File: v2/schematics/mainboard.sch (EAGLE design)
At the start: 145 parts, among them IC1 TEENSY 3.6, IC10 UDN2981A, IC2 LM393, IC3 DRV8835, IC4 LM2596S-ADJ, IC5 LM2596S-5.0, IC6 PCF8574P, IC7 PCF8574P, IC8 LD1117A, IC9 TSOP34830, J1 Servo_1, J10 Uart_5, J11 Servo_3, J12 USB_Host, J13 BNO055, J14 I2C_0 / Uart_3, J15 SPI_1, J16 SPI_2, J17 Uart_6, J18 Maus_select, J19 Erw_analog, J2 Servo_2, J20 Erw_PWM, J21 Erw_GPIO, J23 Uart_1, J24 I2C_3, J3 Erw_Pow, J30 H-Bridge Mode, J4 Uart_2, J5 BPS, J6 Erw_ENA, J7 I2C_2, J8 I2C_Display, J9 RPI_SPI0, Q2 IRL3103, SW1 TL36WO, U1 CNY70, U2 BLE-HM-10, U3 BSS138, U4 BSS138, U5 BSS138, X1 Bat

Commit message: bugfixes for wrong voltage dividers
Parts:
- removed C12: 1uF, rcl:C-EU025-025X050
- removed R47, R48: 2k2, rcl:R-EU_0204/2V
- removed U2: BLE-HM-10, BLE_HM-10:RANDOM-PARTS_BLE-HM-10
- R49, R50: value 3k9 -> 100k
- R51: value 2k2 -> 100k
- R52: value 3k9 -> 180k
- ST7, ST8, ST9: device pinhead_ts:PINHD-1X10 -> pinhead_ts:PS25-10PS25-10
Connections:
- removed net BLE_RESET: J10.4, U2.RESETB
- removed net MLINKS_3V3: IC1.18/A4/PWM/T/SDA0, R47.1, R50.1
- removed net MRECHTS_3V3: IC1.19/A5/PWM/T/SCL0, R48.1, R49.1
- net +3V3: no longer C12.1, U2.3.3V
- net +5V: now also J10.2
- net GND: no longer C12.2, U2.GND1
- net MLINKS: now also IC1.18/A4/PWM/T/SDA0, R50.1; no longer R47.2
- net MRECHTS: now also IC1.19/A5/PWM/T/SCL0, R49.1; no longer R48.2
- net RX5: now also J10.3; no longer J10.2, U2.UART_TX
- net TX5: now also J10.4; no longer J10.3, U2.UART_RX
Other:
- note added: "0.4"
- note added: "BLE / WiFi Modul? Oder Anschluss dafuer?"
- note removed: "0.3"
- note removed: "Interruptfaehigkeit der Eingaenge pruefen!"
- moved on the sheet: J10, J17, J23, J4, J5, R49, R50

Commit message: cleanup of schematic, bugfix wheel encoder circuit
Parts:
- removed L3: 47u, inductors:09HCP
- removed Q2: IRL3103, transistor-power:IRF740
- removed ST7: Maussensor, pinhead_ts:PS25-10PS25-10
- removed ST8: Sensoren L, pinhead_ts:PS25-10PS25-10
- removed ST9: Sensoren R, pinhead_ts:PS25-10PS25-10
- removed SV1: RPI_Interface, con-harting-ml:ML26
- added C12: 100nF, rcl:C-EU025-025X050
- added C18: 220uF, rcl:CPOL-EUE2-5
- added C21, C22: 220n, rcl:C-EU025-025X050
- added C23, C24, C25, C27: 1u, rcl:C-EU025-025X050
- added C26: 220u, rcl:CPOL-EUE2.5-6
- added C28, C30: 2.2nF, rcl:C-EU025-025X050
- added C29, C31: 6.8nF, rcl:C-EU025-025X050
- added C3: 1nF, rcl:C-EU025-025X050
- added IC11: ESP01, esp8266modules:ESP01
- added IC12: MAX803TEXR, maxim-10:MAX803TEXR
- added J22: Erw_GPIO, pinhead_ts:PINHD-1X4
- added J25: Bat_In, pinhead_ts:PINHD-1X2
- added J26: SWD, pinhead_ts:PINHD-1X6
- added J27: SPEAKER, pinhead_ts:PINHD-1X2
- added J28: AUDIO, pinhead_ts:PINHD-1X2
- added J29: GAIN_0, pinhead_ts:PINHD-1X3
- added J31: SWD_KL02, pinhead_ts:PINHD-1X2
- added J32: SWD_KL02, pinhead_ts:PINHD-1X2/90
- added L1: 47u, inductors:09HCP
- added R47, R48: 330, rcl:R-EU_0204/2V
- added ST1: Motor L, pinhead_ts:PINHD-1X2/90
- added ST4: Sensoren R, pinhead_ts:PS25-10PS25-10
- added ST5: RPI_Interface, con-harting-ml:ML26
- added ST6: Maussensor, pinhead_ts:PS25-10PS25-10
- added U2: CNY70, cny70:CNY70
- added U6: TPA3106D1, user:TPA3106D1
- C1: value 220uF -> 680uF; device rcl:CPOL-EUE2-5 -> rcl:CPOL-EUE5-10.5
- C10: value 220u -> 100nF; device rcl:CPOL-EUE5-10.5 -> rcl:C-EU025-025X050
- C11: value 1nF -> 100nF
- C13: value 22uF -> 220uF; device rcl:C-EU025-025X050 -> rcl:CPOL-EUE2-5
- C15: value 220uF -> 100nF; device rcl:CPOL-EUE2-5 -> rcl:C-EU025-025X050
- C16: value 100nF -> 100uF; device rcl:C-EU025-025X050 -> rcl:CPOL-EUE2-5
- C19: value 100uF -> 1u; device rcl:CPOL-EUE2-5 -> rcl:C-EU025-025X050
- C2: value 100nF -> 22uF
- C20: value 10uF -> 10n; device rcl:CPOL-EUE2.5-5 -> rcl:C-EU025-025X050
- C4: value 100nF -> 220u; device rcl:C-EU025-025X050 -> rcl:CPOL-EUE5-10.5
- C6: value 680uF -> 22uF; device rcl:CPOL-EUE5-10.5 -> rcl:C-EU025-025X050
- C8: value 22uF -> 100nF
- C9: value 100nF -> 10uF; device rcl:C-EU025-025X050 -> rcl:CPOL-EUE2.5-5
- IC1: value TEENSY 3.6 -> LM2596S-ADJ; device Teensy_3_6:TEENSY3_6--ALLPINS -> linear:LM2596S
- IC10: value UDN2981A -> TSOP34830; device uln-udn:UDN2981A -> vishay-1:TSOP34830
- IC2: value LM393 -> LM2596S-5.0; device linear:LM393N -> linear:LM2596S; SPICEPREFIX J -> (none)
- IC3: value DRV8835 -> LD1117A; device pololu:POLOLU_MOTOR_DRV8835THROUGHHOLE -> LD1117:LD1117
- IC4: value LM2596S-ADJ -> DRV8835; device linear:LM2596S -> pololu:POLOLU_MOTOR_DRV8835THROUGHHOLE
- IC5: value LM2596S-5.0 -> LM393; device linear:LM2596S -> linear:LM393N; SPICEPREFIX (none) -> J
- IC6: value PCF8574P -> TEENSY 3.6; device micro-philips:PCF8574P -> Teensy_3_6:TEENSY3_6--ALLPINS
- IC8: value LD1117A -> PCF8574P; device LD1117:LD1117 -> micro-philips:PCF8574P
- IC9: value TSOP34830 -> UDN2981A; device vishay-1:TSOP34830 -> uln-udn:UDN2981A
- J1: value Servo_1 -> Erw_Pow; device pinhead_ts:PINHD-1X3 -> pinhead_ts:PINHD-1X4
- J10: value Uart_5 -> I2C_0
- J11: value Servo_3 -> I2C_3
- J12: value USB_Host -> Uart_1
- J13: value BNO055 -> Uart_6; device pinhead_ts:PINHD-1X6 -> pinhead_ts:PINHD-1X4
- J14: value I2C_0 / Uart_3 -> USB_Host
- J15: value SPI_1 -> BPS; device pinhead_ts:PINHD-1X6 -> pinhead_ts:PINHD-1X3
- J16: value SPI_2 -> RPI_SPI0; device pinhead_ts:PINHD-1X5 -> pinhead_ts:PINHD-1X6
- J17: value Uart_6 -> SPI_1; device pinhead_ts:PINHD-1X4 -> pinhead_ts:PINHD-1X6
- J18: value Maus_select -> SPI_2; device pinhead_ts:PINHD-1X3 -> pinhead_ts:PINHD-1X5
- J2: value Servo_2 -> H-Bridge Mode; device pinhead_ts:PINHD-1X4 -> pinhead_ts:PINHD-1X2
- J20: value Erw_PWM -> Erw_Servo; device pinhead_ts:PINHD-1X4 -> pinhead_ts:PINHD-1X3
- J21: value Erw_GPIO -> Erw_PWM; SPICEPREFIX E -> (none)
- J23: value Uart_1 -> Erw_ENA; device pinhead_ts:PINHD-1X4 -> pinhead_ts:PINHD-1X6
- J24: value I2C_3 -> ESP01 Prog; device pinhead_ts:PINHD-1X4 -> pinhead_ts:PINHD-1X3
- J3: value Erw_Pow -> Servo_1; device pinhead_ts:PINHD-1X5 -> pinhead_ts:PINHD-1X3
- J30: value H-Bridge Mode -> GAIN_1; device pinhead_ts:PINHD-1X2 -> pinhead_ts:PINHD-1X3
- J4: value Uart_2 -> Servo_2
- J5: value BPS -> Servo_3; device pinhead_ts:PINHD-1X3 -> pinhead_ts:PINHD-1X4
- J6: value Erw_ENA -> Maus_select; device pinhead_ts:PINHD-1X6 -> pinhead_ts:PINHD-1X3
- J7: value I2C_2 -> BNO055
- J8: value I2C_Display -> Uart_2
- J9: value RPI_SPI0 -> I2C_Display; device pinhead_ts:PINHD-1X6 -> pinhead_ts:PINHD-1X4
- LED1: value blau -> 6V
- LED10: value 6V -> tuerkis
- LED11: value 3.3V -> weiss
- LED2: value blau -> 5V
- LED3: value rot -> 3.3V
- LED4: value orange -> blau
- LED5: value gelb -> blau
- LED6: value gruen -> rot
- LED7: value tuerkis -> orange
- LED8: value weiss -> gelb
- LED9: value 5V -> gruen
- R1, R37, R38, R8: value 4k7 -> 100k
- R10: value 330 -> 100
- R11: value 330 -> 47k
- R12, R13: value 330 -> 470k
- R14: value 330 -> 5k; device rcl:R-EU_0204/2V -> rcl:R-TRIMM64W
- R15: value 330 -> 10k
- R16: value 330 -> 1M
- R17: value 3K9 0.1% -> 10k; device rcl:R-EU_0204/2V -> rcl:R-EU_0204/7
- R18: value 22k -> 15k
- R19: value 5k -> 10k; device rcl:R-TRIMM64W -> rcl:R-EU_0204/2V
- R2: value 100k -> 3K9 0.1%
- R21: value 470k -> 10k
- R22: value 470k -> 1M
- R23: value 210 -> 10k
- R24: value 210 -> 15k
- R25: value 180 -> 10k
- R26: value 180 -> 6,8 2W; device rcl:R-EU_0204/2V -> rcl:R-EU_0204/7
- R27: value 100 -> 4k7
- R28: value 6,8 2W -> 4k7; device rcl:R-EU_0204/7 -> rcl:R-EU_0204/2V
- R29: value 1K 0.1% -> 4k7
- R3: value 100 -> 1K 0.1%
- R30: value 390 -> 210; device resistor:R-EU_0204/2V -> rcl:R-EU_0204/2V
- R31: value 4k7 -> 210
- R32: value 1k8 -> 180
- R33: value 100k -> 180
- R34, R35: value 10k -> 47k
- R36: value 10k -> 100; device rcl:R-EU_0204/7 -> rcl:R-EU_0204/2V
- R39: value 10k -> 1k8
- R4: value 330 -> 390
- R40: value 1k8 -> 4k7; device rcl:R-EU_0204/7 -> rcl:R-EU_0204/2V
- R41: value 1M -> 1k8
- R42: value 1M -> 4k7
- R43: value 10k -> 100k
- R44: value 10k -> 180k
- R45: value 4k7 -> 330; device rcl:R-EU_0204/7 -> rcl:R-EU_0204/2V
- R46: value 4k7 -> 330
- R49, R50, R51: value 100k -> 330
- R5: value 47k -> 330; device rcl:R-EU_0204/2V -> resistor:R-EU_0204/2V
- R52: value 180k -> 330
- R53: value 10k -> 4k7
- R54: value 10k -> 4k7; device rcl:R-EU_0204/7 -> rcl:R-EU_0204/2V
- R55, R56: value 15k -> 10k
- R57: value 120 -> 10k; device resistor:R-EU_0204/2V -> rcl:R-EU_0204/2V
- R59: value 10k -> 5K; device rcl:R-EU_0204/2V -> rcl:R-TRIMM64W
- R6: value 47k -> 120; device rcl:R-EU_0204/2V -> resistor:R-EU_0204/2V
- R60: value 1k -> 100K
- R7: value 47k -> 1k
- R9: value 330 -> 22k
- ST2: value Motor L -> Motor R
- ST3: value Motor R -> Sensoren L; device pinhead_ts:PINHD-1X2/90 -> pinhead_ts:PS25-10PS25-10
- SW1: value TL36WO -> TL32PO; device switch:TL36WO -> switch:TL32PO
- U1: value CNY70 -> IRL3103; device cny70:CNY70 -> transistor-power:IRF740; SPICEPREFIX E -> (none)
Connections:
- removed net A21_DAC0: IC1.DAC0, J19.2
- removed net PWM_ERW: IC1.2/PWM, J20.1
- removed net SCL2: IC1.3/PWM/SCL2/CAN0TX, IC6.SCL, IC7.SCL, J7.6, R8.1, SV1.21, U4.S
- removed net SCL2_5V: J13.5, J8.4, R58.1, SV1.9, U4.D
- removed net SDA2: IC1.4/PWM/SDA2/CAN0RX, IC6.SDA, IC7.SDA, J7.5, R31.1, SV1.19, U3.S
- removed net SDA2_5V: J13.4, J8.3, R59.1, SV1.7, U3.D
- new net 3V3_TEENSY: IC12.VCC, IC6.3V3, J26.1
- new net AUDIO_OUT: IC6.DAC0, J19.2, J28.1
- new net BSN1: C21.1, U6.BSN
- new net BSP1: C22.1, U6.BSP
- new net ESP_GPIO0: IC11.GPIO0, J24.2
- new net ESP_GPIO2: IC11.GPIO2, J24.1
- new net GAIN0: J29.2, U6.GAIN0
- new net GAIN1: J30.2, U6.GAIN1
- new net INN: C24.1, U6.INN
- new net INP: C25.1, U6.INP
- new net KL02_DC: J31.1, J32.1
- new net KL02_DD: J31.2, J32.2
- new net LINE_IN: J28.2, R59.A
- new net N$163: C25.2, R59.S
- new net N$90: U6.FAULT, U6.MUTE
- new net OUTN: C21.2, J27.1, U6.OUTN0, U6.OUTN1
- new net OUTP: C22.2, J27.2, U6.OUTP0, U6.OUTP1
- new net PWM_ERW1: IC6.2/PWM, J21.2
- new net PWM_ERW2: IC6.3/PWM/SCL2/CAN0TX, J21.3
- new net PWM_ERW3: IC6.4/PWM/SDA2/CAN0RX, J21.4
- new net ROSC: R60.2, U6.ROSC
- new net SCL0_5V: J7.5, J9.4, R56.1, ST5.9, U4.D
- new net SDA0_5V: J7.4, J9.3, R55.1, ST5.7, U3.D
- new net SWCLK: IC6.DC, J26.5
- new net SWDIO: IC6.DD, J26.6
- new net SWD_EN: IC6.DE, J26.4
- new net VBYP: C19.1, U6.VBYP
- new net VCLAMP1: C23.1, U6.VCLAMP
- new net VREG: C20.1, J29.1, J30.1, U6.MSTR/SLV, U6.VREG
- net +3V3: now also C17.1, C9.+, IC10.VS, IC11.CH_PD, IC11.VCC, IC3.VOUT, J1.2, J15.3, J6.3, R11.1, R12.1, R13.1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; no longer C20.+, IC8.VOUT, IC9.VS, J18.3, J3.2, J5.3, R1.1, R19.E, R21.1, R22.1, R31.2, R35.2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
- net +5V: now also C12.1, C13.+, C15.1, C16.+, C18.+, C8.1, IC2.FB, IC3.VIN, IC4.VCC, IC5P.V+, IC6.VIN, IC8.A0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; no longer C1.+, C15.+, C19.+, C2.1, C4.1, C9.1, IC1.VIN, IC10.VS, IC2P.V+, IC3.VCC, IC5.FB, IC6.VDD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
- net +6V: now also C3.1, C4.+, IC4.VIN, J1.3, L1.2, R2.2, R26.1, R4.1; no longer C10.+, C11.1, IC3.VIN, J3.3, L2.2, R17.2, R28.1, R30.1
- net A22_DAC1: now also IC6.DAC1; no longer IC1.DAC1
- net ABSTL: now also R39.2, ST3.4; no longer R32.2, ST8.4
- net ABSTL_3V3: now also IC6.A11, R39.1, R40.1; no longer IC1.A11, R32.1, R46.1
- net ABSTR: now also R41.2, ST4.4; no longer R40.2, ST9.4
- net ABSTR_3V3: now also IC6.A10, R41.1, R42.1; no longer IC1.A10, R40.1, R45.1
- net BAT+: now also R1.1, X1-2.KL; no longer R33.1, X1-1.KL
- net BAT-: now also U1.D, X1-1.KL; no longer Q2.D, X1-2.KL
- net BAT_IN: now also C1.+, C2.1, C26.+, C27.1, C6.1, IC1.IN, IC2.IN, J25.1, R8.1, U6.!SHUTDOWN, U6.AVCC, U6.PVCC0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; no longer C13.1, C6.+, C8.1, IC4.IN, IC5.IN, J3.5, R2.1
- net BAT_IN_FB: now also IC6.39/A20/ALT-MISO0, R7.1; no longer IC1.39/A20/ALT-MISO0, R60.1
- net BPS: now also IC6.51/MISO2, J15.1; no longer IC1.51/MISO2, J5.1
- net CS0: now also IC6.15/A1/CS0-4/T, ST5.8; no longer IC1.15/A1/CS0-4/T, SV1.8
- net CS1: now also IC6.31/A12/PWM/RX4/CS1-0, J17.3; no longer IC1.31/A12/PWM/RX4/CS1-0, J15.3
- net CS2: now also IC6.43/CS2-0, J18.2; no longer IC1.43/CS2-0, J16.2
- net DRV_ABSTAND: now also IC9.O1, ST3.3, ST4.3; no longer IC10.O1, ST8.3, ST9.3
- net DRV_ERW_1: now also IC9.O7, J23.4; no longer IC10.O7, J6.4
- net DRV_ERW_2: now also IC9.O8, J23.6; no longer IC10.O8, J6.6
- net DRV_KANTLED: now also IC9.O4, R32.2, R33.1; no longer IC10.O4, R25.2, R26.1
- net DRV_KLAPPLED: now also IC9.O5, R10.2; no longer IC10.O5, R27.2
- net DRV_MAUS: now also IC9.O6, ST6.9; no longer IC10.O6, ST7.9
- net DRV_RADLED: now also IC9.O2, R30.2, R31.1; no longer IC10.O2, R23.2, R24.1
- net DRV_SCHRANKE: now also IC9.O3, ST3.7; no longer IC10.O3, ST8.7
- net ENA_ABSTAND: now also IC8.P0, IC9.I1; no longer IC10.I1, IC7.P0
- net ENA_ERW_1: now also IC8.P6, IC9.I7, J23.3; no longer IC10.I7, IC7.P6, J6.3
- net ENA_ERW_2: now also IC8.P7, IC9.I8, J23.5; no longer IC10.I8, IC7.P7, J6.5
- net ENA_KANTLED: now also IC8.P3, IC9.I4; no longer IC10.I4, IC7.P3
- net ENA_KLAPPLED: now also IC8.P4, IC9.I5; no longer IC10.I5, IC7.P4
- net ENA_MAUS: now also IC8.P5, IC9.I6; no longer IC10.I6, IC7.P5
- net ENA_RADLED: now also IC8.P1, IC9.I2; no longer IC10.I2, IC7.P1
- net ENA_SCHRANKE: now also IC8.P2, IC9.I3; no longer IC10.I3, IC7.P2
- net ENCL: now also R17.1, R18.2, ST3.1; no longer R36.1, R56.2, ST8.1
- net ENCR: now also R23.1, R24.2, ST4.1; no longer R39.1, R55.2, ST9.1
- net FERNBED: now also IC10.OUT, IC6.28/ALT-MOSI0; no longer IC1.28/ALT-MOSI0, IC9.OUT
- net GND: now also C10.2, C11.2, C12.2, C13.-, C15.2, C16.-, C18.-, C19.2, C20.2, C23.2, C24.2, C26.-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; no longer C10.-, C13.2, C15.-, C16.2, C19.-, C20.-, C4.2, C6.-, C9.2, IC1.AGND, IC2P.V-, IC3.LGND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
- net GPIO40: now also IC6.40, J22.1; no longer IC1.40, J21.1
- net GPIO41: now also IC6.41, J22.2; no longer IC1.41, J21.2
- net GPIO42: now also IC6.42, J18.1, J22.3; no longer IC1.42, J16.1, J21.3
- net KANTEL: now also IC6.16/A2/PWM/T/ALT-SCL0, R34.1, ST3.6; no longer IC1.16/A2/PWM/T/ALT-SCL0, R5.1, ST8.6
- net KANTER: now also IC6.17/A3/PWM/T/ALT-SDA0, R35.2, ST4.6; no longer IC1.17/A3/PWM/T/ALT-SDA0, R6.2, ST9.6
- net KLAPPE: now also IC6.55, R11.2, U2.COL; no longer IC1.55, R7.2, U1.COL
- net KLAPPLED: now also R10.1, U2.A; no longer R27.1, U1.A
- net LDRL: now also IC6.37/A18/PWM/SCL1, R13.2; no longer IC1.37/A18/PWM/SCL1, R21.2
- net LDRR: now also IC6.38/A19/PWM/SDA1, R12.2; no longer IC1.38/A19/PWM/SDA1, R22.2
- net MAUS_CLK: now also IC6.52/MOSI2, ST6.4; no longer IC1.52/MOSI2, ST7.4
- net MAUS_D_3V3: now also IC6.53/PWM/SCK2, J22.4, R57.2; no longer IC1.53/PWM/SCK2, J21.4, R53.2
- net MAUS_SDIO: now also J6.2, ST6.2; no longer J18.2, ST7.2
- net MISO0: now also IC6.12/MISO0, J16.5, ST5.4; no longer IC1.12/MISO0, J9.5, SV1.4
- net MISO1: now also IC6.1/TX1/MISO1/T, J17.5, ST6.6; no longer IC1.1/TX1/MISO1/T, J15.5, ST7.6
- net MISO2: now also IC6.45/CS0-5/MISO2, J18.4; no longer IC1.45/CS0-5/MISO2, J16.4
- net MLINKS: now also IC6.18/A4/PWM/T/SDA0, R37.1, ST6.7; no longer IC1.18/A4/PWM/T/SDA0, R50.1, ST7.7
- net MOSI0: now also IC6.11/MOSI0, J16.4, ST5.2; no longer IC1.11/MOSI0, J9.4, SV1.2
- net MOSI1: now also IC6.0/RX1/MOSI1/T, J17.4, ST6.5; no longer IC1.0/RX1/MOSI1/T, J15.4, ST7.5
- net MOSI2: now also IC6.44/MOSI2, J18.3; no longer IC1.44/MOSI2, J16.3
- net MOT_L_1: now also IC4.AOUT1, ST1.1; no longer IC3.AOUT1, ST2.1
- net MOT_L_2: now also IC4.AOUT2, ST1.2; no longer IC3.AOUT2, ST2.2
- net MOT_L_DIR: now also IC4.APHASE, IC6.29/PWM/T/ALT-CAN0TX; no longer IC1.29/PWM/T/ALT-CAN0TX, IC3.APHASE
- net MOT_L_PWM: now also IC4.AENBL, IC6.35/A16/PWM; no longer IC1.35/A16/PWM, IC3.AENBL
- net MOT_R_1: now also IC4.BOUT1, ST2.1; no longer IC3.BOUT1, ST3.1
- net MOT_R_2: now also IC4.BOUT2, ST2.2; no longer IC3.BOUT2, ST3.2
- net MOT_R_DIR: now also IC4.BPHASE, IC6.30/PWM/T/ALT-CAN0RX; no longer IC1.30/PWM/T/ALT-CAN0RX, IC3.BPHASE
- net MOT_R_PWM: now also IC4.BENBL, IC6.36/A17/PWM; no longer IC1.36/A17/PWM, IC3.BENBL
- net MRECHTS: now also IC6.19/A5/PWM/T/SCL0, R38.1, ST6.8; no longer IC1.19/A5/PWM/T/SCL0, R49.1, ST7.8
- net N$1: now also R36.1, ST4.7; no longer R3.1, ST9.7
- net N$10: now also IC5A.+IN, R15.2, R16.1; no longer IC2A.+IN, R42.1, R43.2
- net N$12: now also IC5B.+IN, R21.2, R22.1; no longer IC2B.+IN, R41.1, R44.2
- net N$13: now also IC5A.-IN, R17.2; no longer IC2A.-IN, R36.2
- net N$14: now also IC5B.-IN, R23.2; no longer IC2B.-IN, R39.2
- net N$16: now also IC7.P4, R49.1; no longer IC6.P4, R13.1
- net N$17: now also IC7.P3, R48.1; no longer IC6.P3, R12.1
- net N$18: now also IC7.P2, R47.1; no longer IC6.P2, R11.1
- net N$19: now also IC7.P1, R46.1; no longer IC6.P1, R10.1
- net N$2: now also LED3.A, R6.2; no longer LED11.A, R57.2
- net N$20: now also IC7.P0, R45.1; no longer IC6.P0, R9.1
- net N$21: now also IC7.P5, R50.1; no longer IC6.P5, R14.1
- net N$22: now also IC7.P6, R51.1; no longer IC6.P6, R15.1
- net N$23: now also IC7.P7, R52.1; no longer IC6.P7, R16.1
- net N$25: now also LED11.C, R52.2; no longer LED8.C, R16.2
- net N$26: now also LED4.C, R45.2; no longer LED1.C, R9.2
- net N$27: now also LED5.C, R46.2; no longer LED2.C, R10.2
- net N$28: now also LED6.C, R47.2; no longer LED3.C, R11.2
- net N$29: now also LED7.C, R48.2; no longer LED4.C, R12.2
- net N$3: now also IC4.MODE, J2.2; no longer IC3.MODE, J30.2
- net N$30: now also LED8.C, R49.2; no longer LED5.C, R13.2
- net N$31: now also LED9.C, R50.2; no longer LED6.C, R14.2
- net N$32: now also LED10.C, R51.2; no longer LED7.C, R15.2
- net N$35: now also C10.1, R14.S, R15.1; no longer C16.1, R19.S, R43.1
- net N$38: now also R1.2, U1.G; no longer Q2.G, R33.2
- net N$39: now also C11.1, R21.1; no longer C17.1, R44.1
- net N$4: now also R7.2, R8.2, R9.1; no longer R18.1, R2.2, R60.2
- net N$45: now also R31.2, ST4.2; no longer R24.2, ST9.2
- net N$47: now also R30.1, ST3.2; no longer R23.1, ST8.2
- net N$5: now also C3.2, IC1.FB, R2.1, R3.2; no longer C11.2, IC4.FB, R17.1, R29.2
- net N$51: now also R32.1, ST3.5; no longer R25.1, ST8.5
- net N$53: now also R33.2, ST4.5; no longer R26.2, ST9.5
- net N$57: now also ST3.8, ST4.8; no longer ST8.8, ST9.8
- net N$6: now also LED2.A, R5.2; no longer LED9.A, R4.2
- net N$8: now also LED1.A, R4.2; no longer LED10.A, R30.2
- net PWM1: now also IC6.5/PWM/ALT-TX1/ALT-MISO1, J3.3, R27.2; no longer IC1.5/PWM/ALT-TX1/ALT-MISO1, J1.3, R38.2
- net PWM2: now also IC6.6/PWM, J4.3, R28.2, ST5.18; no longer IC1.6/PWM, J2.3, R37.2, SV1.18
- net PWM3: now also IC6.20/A6/PWM/CS0-2/ALT-SCK1, J5.3, R29.2, ST5.16; no longer IC1.20/A6/PWM/CS0-2/ALT-SCK1, J11.3, R1.2, SV1.16
- net PWM4: now also IC6.21/A7/PWM/CS0-3/ALT-MOSI1/ALT-RX1, J20.3; no longer IC1.21/A7/PWM/CS0-3/ALT-MOSI1/ALT-RX1, J20.4
- net PWM5: now also IC6.22/A8/PWM/T, J20.2; no longer IC1.22/A8/PWM/T, J20.3
- net PWM6: now also IC6.23/A9/PWM/T, J20.1; no longer IC1.23/A9/PWM/T, J20.2
- net PWR_SERVO: now also J3.2, J4.2, J5.2, R26.2, ST5.22; no longer J1.2, J11.2, J2.2, R28.2, SV1.22
- net RADL: now also C30.1, C31.1, IC5A.OUT, IC6.24, R16.2, R19.1; no longer IC1.24, IC2A.OUT, R34.1, R42.2
- net RADR: now also C28.1, C29.1, IC5B.OUT, IC6.25, R22.2, R25.1; no longer IC1.25, IC2B.OUT, R35.1, R41.2
- net RESET: now also IC12./RST, IC6.RESET, J26.2, ST5.12; no longer IC1.RESET, SV1.12
- net RPI_3V3: now also J16.2, ST5.11; no longer J9.2, SV1.11
- net RPI_SPI0_CE1: now also J16.3, ST5.10; no longer J9.3, SV1.10
- net RX1: now also IC6.27/ALT-RX1/ALT-SCK0, J12.4, ST5.15; no longer IC1.27/ALT-RX1/ALT-SCK0, J23.4, SV1.15
- net RX2: now also IC6.9/PWM/RX2/CS0-1, J8.4; no longer IC1.9/PWM/RX2/CS0-1, J4.4
- net RX5: now also IC11.TXD, IC6.34/A15/CAN1RX/RX5/ALT-SDA0; no longer IC1.34/A15/CAN1RX/RX5/ALT-SDA0, J10.3
- net RX6: now also IC6.47/SCL0/RX6, J13.4; no longer IC1.47/SCL0/RX6, J17.4
- net SCHRANKE: now also R43.2, ST3.9; no longer R51.2, ST8.9
- net SCHRANKE_3V3: now also IC6.54/CS2-1, R43.1, R44.1; no longer IC1.54/CS2-1, R51.1, R52.1
- net SCK0: now also IC6.14/A0/PWM/ALT-SCK0, J16.6, ST5.6; no longer IC1.14/A0/PWM/ALT-SCK0, J9.6, SV1.6
- net SCK1: now also IC6.32/A13/PWM/TX4/SCK1, J17.6, ST6.3; no longer IC1.32/A13/PWM/TX4/SCK1, J15.6, ST7.3
- net SCK2: now also IC6.46/SCK2, J18.5; no longer IC1.46/SCK2, J16.5
- net SCL0: now also IC6.7/PWM/RX3/ALT-SCL0/ALT-MOSI0, IC7.SCL, IC8.SCL, J10.4, R54.1, ST5.21, U4.S; no longer IC1.7/PWM/RX3/ALT-SCL0/ALT-MOSI0, J14.4
- net SCL3: now also IC6.57/SCL3, J11.3; no longer IC1.57/SCL3, J24.3
- net SDA0: now also IC6.8/PWM/TX3/ALT-SDA0/ALT-MISO0, IC7.SDA, IC8.SDA, J10.3, R53.1, ST5.19, U3.S; no longer IC1.8/PWM/TX3/ALT-SDA0/ALT-MISO0, J14.3
- net SDA3: now also IC6.56/SDA3, J11.4; no longer IC1.56/SDA3, J24.4
- net SDIO_5V: now also J6.1, R58.2; no longer J18.1, R54.2
- net SERVO2_FB: now also IC6.49/A23/PWM, J4.4, ST5.20; no longer IC1.49/A23/PWM, J2.4, SV1.20
- net SERVO3_FB: now also IC6.50/A24/PWM, J5.4, ST5.14; no longer IC1.50/A24/PWM, J11.4, SV1.14
- net TX1: now also IC6.26/ALT-PWM/ALT-TX1/ALT-SCL2, J12.3, ST5.17; no longer IC1.26/ALT-PWM/ALT-TX1/ALT-SCL2, J23.3, SV1.17
- net TX2: now also IC6.10/PWM/TX2/CS0-0, J8.3; no longer IC1.10/PWM/TX2/CS0-0, J4.3
- net TX5: now also IC11.RXD, IC6.33/A14/CAN1TX/TX5/ALT-SCL0; no longer IC1.33/A14/CAN1TX/TX5/ALT-SCL0, J10.4
- net TX6: now also IC6.48/SDA0/TX6, J13.3; no longer IC1.48/SDA0/TX6, J17.3
- net USB1_D+: now also IC6.D+, J14.3; no longer IC1.D+, J12.3
- net USB1_D-: now also IC6.D-, J14.2; no longer IC1.D-, J12.2
- net V5_L1: now also D2.C, IC2.OUT, L2.1; no longer D1.C, IC5.OUT, L3.1
- net V6_L1: now also D1.C, IC1.OUT, L1.1; no longer D2.C, IC4.OUT, L2.1
- net VBAT_RTC: now also IC6.VBAT; no longer IC1.VBAT
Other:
- note added: "(oder ähnlicher Reset-Controller)"
- note added: "AUDIO"
- note added: "BPS"
- note added: "ERWEITERUNGEN"
- note added: "I2C"
- note added: "RPI INTERFACE"
- note added: "RTC BATTERIE"
- note added: "Rev. 0.5"
- note added: "SERVO"
- note added: "SPI"
- note added: "SWD DEBUG PORT"
- note added: "UART"
- note added: "USB HOST"
- note added: "USB2Bot / Wi-Fi"
- note added: "WIFI"
- note added: "Wi-Fi Modul?"
- note added: "c't-Bot Hauptplatine v2 (optionale Parts) !!! UNTESTED DRAFT !!!"
- note added: "mainboard"
- note removed: "0.4"
- note removed: "BLE / WiFi Modul? Oder Anschluss dafuer?"
- note removed: "Schaltung checken! Widerstandswerte pruefen!"
- note removed: "USB2Bot / WiFi"

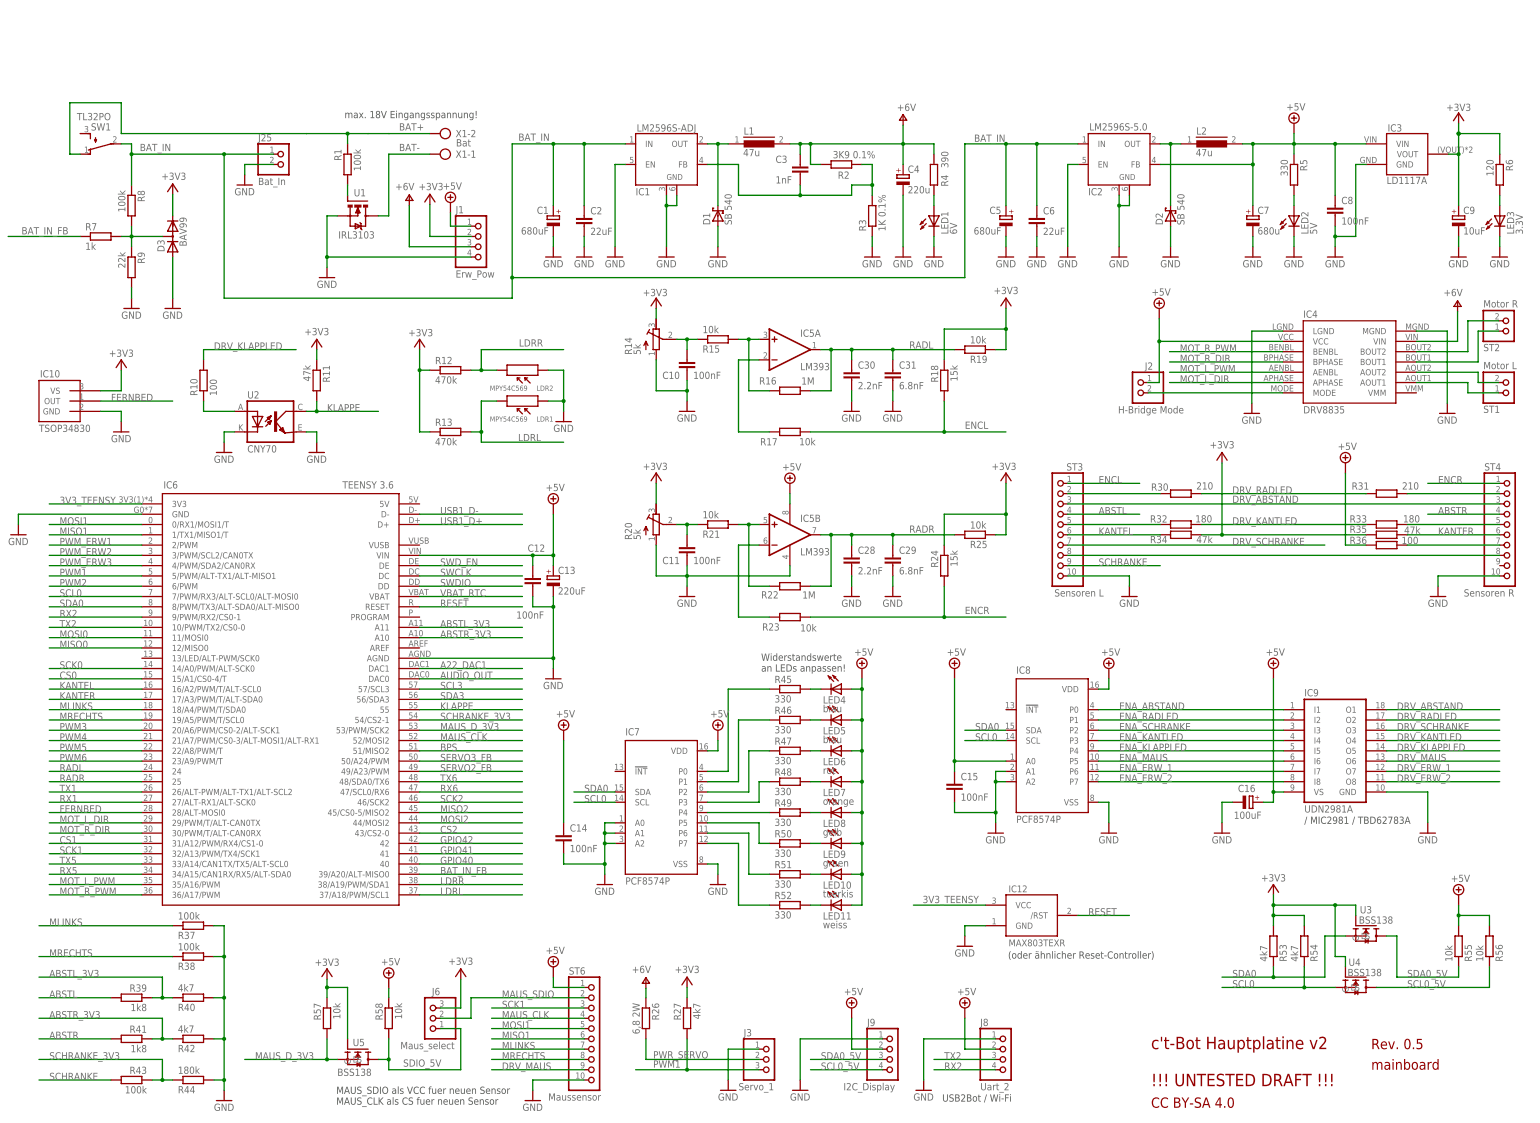
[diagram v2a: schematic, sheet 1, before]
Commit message: Updated schematics to Revision 0.6.
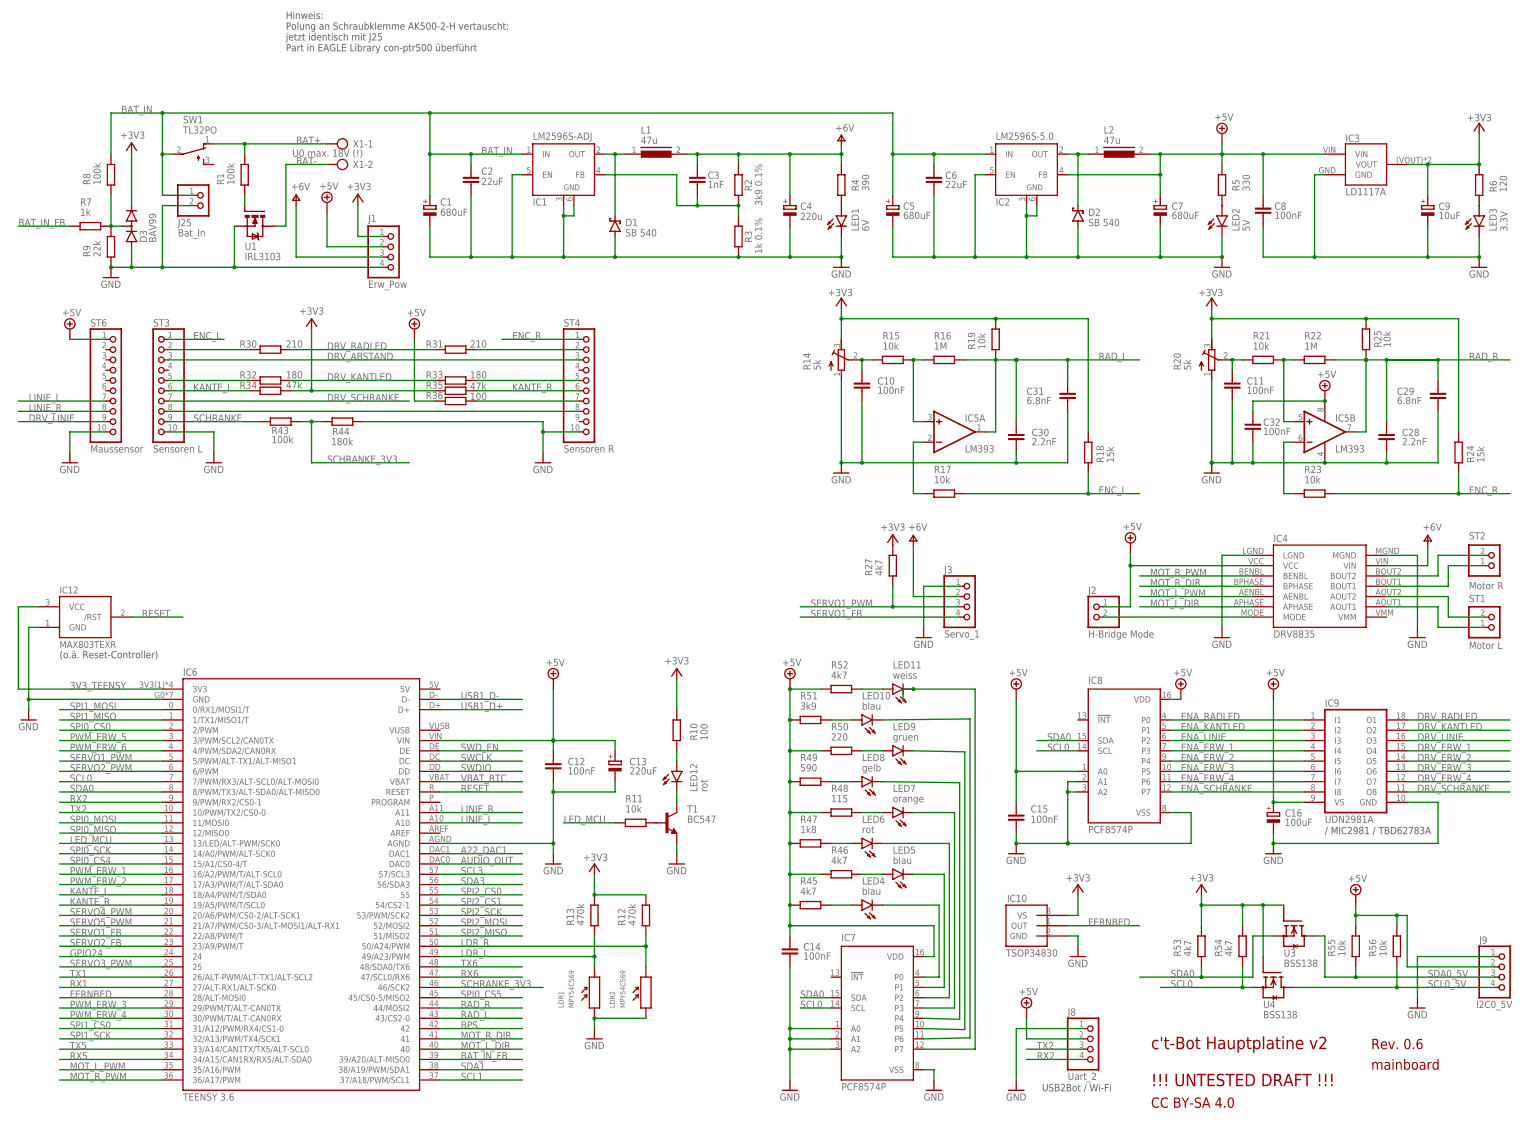
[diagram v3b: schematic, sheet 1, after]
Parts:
- removed IC11: ESP01, esp8266modules:ESP01
- removed J22: Erw_GPIO, pinhead_ts:PINHD-1X4
- removed R38: 100k, rcl:R-EU_0204/2V
- removed R39, R41: 1k8, rcl:R-EU_0204/2V
- removed R40, R42: 4k7, rcl:R-EU_0204/2V
- removed R57, R58: 10k, rcl:R-EU_0204/2V
- removed R59: 5K, rcl:R-TRIMM64W
- removed R60: 100K, rcl:R-EU_0204/2V
- removed U2: CNY70, cny70:CNY70
- removed U5: BSS138, Ava:BSS138
- added C32: 100nF, rcl:C-EU025-025X050
- added ESP-01: WIRELESS-WIFI-ESP-01, DIYmodules-general:WIRELESS-WIFI-ESP-01
- added ESP-12: ESP-12, adafruit:ESP-12
- added J33: Erw_Servo, DIYmodules-pinhead:PINHD-1X2
- added LED12: rot, led:LED3MM
- added T1: BC547, transistor:BC547
- C13, C16, C18: device rcl:CPOL-EUE2-5 -> rcl:CPOL-EUE5-10.5
- C26: device rcl:CPOL-EUE2.5-6 -> rcl:CPOL-EUE5-10.5
- C7: value 680u -> 680uF
- C9: device rcl:CPOL-EUE2.5-5 -> rcl:CPOL-EUE5-10.5
- IC12: device maxim-10:MAX803TEXR -> EAGLE-maxim-10:MAX803TEXR
- J1, J10, J11, J12, J14, J4, J5, J8: device pinhead_ts:PINHD-1X4 -> DIYmodules-pinhead:PINHD-1X4
- J13: value Uart_6 -> Uart_6 (LP); device pinhead_ts:PINHD-1X4 -> DIYmodules-pinhead:PINHD-1X4
- J15, J24, J29, J30: device pinhead_ts:PINHD-1X3 -> DIYmodules-pinhead:PINHD-1X3
- J16: value RPI_SPI0 -> SPI0; device pinhead_ts:PINHD-1X6 -> DIYmodules-pinhead:PINHD-1X8
- J17, J26, J7: device pinhead_ts:PINHD-1X6 -> DIYmodules-pinhead:PINHD-1X6
- J18: device pinhead_ts:PINHD-1X5 -> DIYmodules-pinhead:PINHD-1X7
- J19, J2, J25, J27, J28, J31: device pinhead_ts:PINHD-1X2 -> DIYmodules-pinhead:PINHD-1X2
- J20: value Erw_Servo -> Erw_GPIO; device pinhead_ts:PINHD-1X3 -> DIYmodules-pinhead:PINHD-1X2
- J21: device pinhead_ts:PINHD-1X4 -> DIYmodules-pinhead:PINHD-1X6
- J23: device pinhead_ts:PINHD-1X6 -> DIYmodules-pinhead:PINHD-1X8
- J3: device pinhead_ts:PINHD-1X3 -> DIYmodules-pinhead:PINHD-1X4
- J32, ST1, ST2: device pinhead_ts:PINHD-1X2/90 -> DIYmodules-pinhead:PINHD-1X2
- J6: value Maus_select -> I2C_1; device pinhead_ts:PINHD-1X3 -> DIYmodules-pinhead:PINHD-1X4
- J9: value I2C_Display -> I2C0_5V; device pinhead_ts:PINHD-1X4 -> DIYmodules-pinhead:PINHD-1X4
- LED10: value tuerkis -> blau
- R11: value 47k -> 10k
- R2: value 3K9 0.1% -> 3k9 0.1%
- R26: value 6,8 2W -> 100k; device rcl:R-EU_0204/7 -> rcl:R-EU_0204/2V
- R3: value 1K 0.1% -> 1k 0.1%
- R37: value 100k -> 5k; device rcl:R-EU_0204/2V -> rcl:R-TRIMM64W
- R4, R5, R6: device resistor:R-EU_0204/2V -> rcl:R-EU_0204/2V
- R45, R46, R52: value 330 -> 4k7
- R47: value 330 -> 1k8
- R48: value 330 -> 115
- R49: value 330 -> 590
- R50: value 330 -> 220
- R51: value 330 -> 3k9
- ST3, ST4, ST6: device pinhead_ts:PS25-10PS25-10 -> DIYmodules-pinhead:PINHD-1X10
- U3, U4: device Ava:BSS138 -> DIYmodules-m-pad-2.1:BSS138
- X1: value Bat -> U0 max. 18V (!); device mylib:SCHRAUBKLEMME/2 -> con-ptr500:AK500/2-H
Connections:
- net BSN1 renamed N$31
- net BSP1 renamed N$32
- net VCLAMP1 renamed N$33
- removed net ABSTL: R39.2, ST3.4
- removed net ABSTL_3V3: IC6.A11, R39.1, R40.1
- removed net ABSTR: R41.2, ST4.4
- removed net ABSTR_3V3: IC6.A10, R41.1, R42.1
- removed net CS0: IC6.15/A1/CS0-4/T, ST5.8
- removed net CS1: IC6.31/A12/PWM/RX4/CS1-0, J17.3
- removed net CS2: IC6.43/CS2-0, J18.2
- removed net DRV_KLAPPLED: IC9.O5, R10.2
- removed net DRV_MAUS: IC9.O6, ST6.9
- removed net ENA_ABSTAND: IC8.P0, IC9.I1
- removed net ENA_KLAPPLED: IC8.P4, IC9.I5
- removed net ENA_MAUS: IC8.P5, IC9.I6
- removed net ENCL: R17.1, R18.2, ST3.1
- removed net ENCR: R23.1, R24.2, ST4.1
- removed net GPIO40: IC6.40, J22.1
- removed net GPIO41: IC6.41, J22.2
- removed net GPIO42: IC6.42, J18.1, J22.3
- removed net KANTEL: IC6.16/A2/PWM/T/ALT-SCL0, R34.1, ST3.6
- removed net KANTER: IC6.17/A3/PWM/T/ALT-SDA0, R35.2, ST4.6
- removed net KLAPPE: IC6.55, R11.2, U2.COL
- removed net KLAPPLED: R10.1, U2.A
- removed net LDRL: IC6.37/A18/PWM/SCL1, LDR1.P$2, R13.2
- removed net LDRR: IC6.38/A19/PWM/SDA1, LDR2.P$2, R12.2
- removed net MAUS_CLK: IC6.52/MOSI2, ST6.4
- removed net MAUS_D_3V3: IC6.53/PWM/SCK2, J22.4, R57.2, U5.S
- removed net MAUS_SDIO: J6.2, ST6.2
- removed net MISO0: IC6.12/MISO0, J16.5, ST5.4
- removed net MISO1: IC6.1/TX1/MISO1/T, J17.5, ST6.6
- removed net MISO2: IC6.45/CS0-5/MISO2, J18.4
- removed net MLINKS: IC6.18/A4/PWM/T/SDA0, R37.1, ST6.7
- removed net MOSI0: IC6.11/MOSI0, J16.4, ST5.2
- removed net MOSI1: IC6.0/RX1/MOSI1/T, J17.4, ST6.5
- removed net MOSI2: IC6.44/MOSI2, J18.3
- removed net MRECHTS: IC6.19/A5/PWM/T/SCL0, R38.1, ST6.8
- removed net N$31 (its old number): LED9.C, R50.2
- removed net N$32 (its old number): LED10.C, R51.2
- removed net PWM1: IC6.5/PWM/ALT-TX1/ALT-MISO1, J3.3, R27.2
- removed net PWM2: IC6.6/PWM, J4.3, R28.2, ST5.18
- removed net PWM3: IC6.20/A6/PWM/CS0-2/ALT-SCK1, J5.3, R29.2, ST5.16
- removed net PWM4: IC6.21/A7/PWM/CS0-3/ALT-MOSI1/ALT-RX1, J20.3
- removed net PWM5: IC6.22/A8/PWM/T, J20.2
- removed net PWM6: IC6.23/A9/PWM/T, J20.1
- removed net PWM_ERW1: IC6.2/PWM, J21.2
- removed net PWM_ERW2: IC6.3/PWM/SCL2/CAN0TX, J21.3
- removed net PWM_ERW3: IC6.4/PWM/SDA2/CAN0RX, J21.4
- removed net RADL: C30.1, C31.1, IC5A.OUT, IC6.24, R16.2, R19.1
- removed net RADR: C28.1, C29.1, IC5B.OUT, IC6.25, R22.2, R25.1
- removed net RPI_3V3: J16.2, ST5.11
- removed net RPI_SPI0_CE1: J16.3, ST5.10
- removed net SCK0: IC6.14/A0/PWM/ALT-SCK0, J16.6, ST5.6
- removed net SCK1: IC6.32/A13/PWM/TX4/SCK1, J17.6, ST6.3
- removed net SCK2: IC6.46/SCK2, J18.5
- removed net SDIO_5V: J6.1, R58.2, U5.D
- removed net SERVO3_FB: IC6.50/A24/PWM, J5.4, ST5.14
- new net DRV_ERW_3: IC9.O6, J23.6
- new net DRV_ERW_4: IC9.O7, J23.8
- new net DRV_LINIE: IC9.O3, ST6.9
- new net ENA_ERW_3: IC8.P5, IC9.I6, J23.5
- new net ENA_ERW_4: IC8.P6, IC9.I7, J23.7
- new net ENA_LINIE: IC8.P2, IC9.I3
- new net ENC_L: R17.2, R18.1, ST3.1
- new net ENC_R: R23.2, R24.1, ST4.1
- new net GPIO24: IC6.24, J20.1
- new net KANTE_L: IC6.18/A4/PWM/T/SDA0, R34.1, ST3.6
- new net KANTE_R: IC6.19/A5/PWM/T/SCL0, R35.2, ST4.6
- new net LDR_L: IC6.49/A23/PWM, LDR1.P$2, R13.1
- new net LDR_R: IC6.50/A24/PWM, LDR2.P$2, R12.1
- new net LED_MCU: IC6.13/LED/ALT-PWM/SCK0, R11.1
- new net LINIE_L: IC6.A10, ST6.7
- new net LINIE_R: IC6.A11, ST6.8
- new net N$11: LED2.A, R5.1
- new net N$15: IC7.P3, LED7.C
- new net N$24: LED7.A, R48.2
- new net N$5: IC5A.-IN, R17.1
- new net N$7: IC7.P1, LED5.C
- new net PWM_ERW_1: IC6.16/A2/PWM/T/ALT-SCL0, J21.1
- new net PWM_ERW_2: IC6.17/A3/PWM/T/ALT-SDA0, J21.2
- new net PWM_ERW_3: IC6.29/PWM/T/ALT-CAN0TX, J21.3
- new net PWM_ERW_4: IC6.30/PWM/T/ALT-CAN0RX, J21.4
- new net PWM_ERW_5: IC6.3/PWM/SCL2/CAN0TX, J21.5
- new net PWM_ERW_6: IC6.4/PWM/SDA2/CAN0RX, J21.6
- new net RAD_L: C30.1, C31.1, IC5A.OUT, IC6.43/CS2-0, R16.2, R19.1
- new net RAD_R: C28.1, C29.1, IC5B.OUT, IC6.44/MOSI2, R22.2, R25.1
- new net SCL1: IC6.37/A18/PWM/SCL1, J6.4
- new net SDA1: IC6.38/A19/PWM/SDA1, J6.3
- new net SERVO1_FB: IC6.22/A8/PWM/T, J3.4
- new net SERVO1_PWM: IC6.5/PWM/ALT-TX1/ALT-MISO1, J3.3, R27.1
- new net SERVO2_PWM: IC6.6/PWM, J4.3, R28.1, ST5.18
- new net SERVO3_PWM: IC6.25, J5.3, R29.1
- new net SERVO4_PWM: IC6.20/A6/PWM/CS0-2/ALT-SCK1, J33.1
- new net SERVO5_PWM: IC6.21/A7/PWM/CS0-3/ALT-MOSI1/ALT-RX1, J33.2
- new net SPI0_CS0: IC6.2/PWM, J16.3
- new net SPI0_CS4: IC6.15/A1/CS0-4/T, J16.4
- new net SPI0_CS5: IC6.45/CS0-5/MISO2, J16.5
- new net SPI0_MISO: IC6.12/MISO0, J16.7
- new net SPI0_MOSI: IC6.11/MOSI0, J16.6
- new net SPI0_SCK: IC6.14/A0/PWM/ALT-SCK0, J16.8
- new net SPI1_CS0: IC6.31/A12/PWM/RX4/CS1-0, J17.3, ST5.8
- new net SPI1_MISO: IC6.1/TX1/MISO1/T, J17.5, ST5.2
- new net SPI1_MOSI: IC6.0/RX1/MOSI1/T, J17.4, ST5.4
- new net SPI1_SCK: IC6.32/A13/PWM/TX4/SCK1, J17.6, ST5.6
- new net SPI2_CS0: IC6.55, J18.3
- new net SPI2_CS1: IC6.54/CS2-1, J18.4
- new net SPI2_MISO: IC6.51/MISO2, J18.6
- new net SPI2_MOSI: IC6.52/MOSI2, J18.5
- new net SPI2_SCK: IC6.53/PWM/SCK2, J18.7
- net +3V3: now also ESP-01.CH_PD, ESP-01.VCC, ESP-12.CH_PD, ESP-12.VCC, J1.1, R10.2, R12.2, R13.2, R18.2, R24.2, R27.2, R28.2, R29.2, R6.2; no longer IC11.CH_PD, IC11.VCC, J1.2, J6.3, R11.1, R12.1, R13.1, R18.1, R24.1, R27.1, R28.1, R29.1, R57.1, R6.1, U5.G
- net +5V: now also C32.1, J1.2, J16.1, J18.2, J6.2, R36.1, R45.1, R46.1, R47.1, R48.1, R49.1, R5.2, R50.1, R51.1, R52.1; no longer J1.1, J23.2, LED10.A, LED11.A, LED4.A, LED5.A, LED6.A, LED7.A, LED8.A, LED9.A, R36.2, R5.1, R58.1
- net +6V: now also J3.2; no longer R26.1
- net BAT+: now also R1.2, X1-1.KL; no longer R1.1, X1-2.KL
- net BAT-: now also X1-2.KL; no longer X1-1.KL
- net BAT_IN: now also R8.2; no longer R8.1
- net BPS: now also IC6.42; no longer IC6.51/MISO2
- net DRV_ABSTAND: no longer IC9.O1
- net DRV_ERW_1: now also IC9.O4, J23.2; no longer IC9.O7, J23.4
- net DRV_ERW_2: now also IC9.O5, J23.4; no longer IC9.O8, J23.6
- net DRV_KANTLED: now also IC9.O2; no longer IC9.O4
- net DRV_RADLED: now also IC9.O1; no longer IC9.O2
- net DRV_SCHRANKE: now also IC9.O8; no longer IC9.O3
- net ENA_ERW_1: now also IC8.P3, IC9.I4, J23.1; no longer IC8.P6, IC9.I7, J23.3
- net ENA_ERW_2: now also IC8.P4, IC9.I5, J23.3; no longer IC8.P7, IC9.I8, J23.5
- net ENA_KANTLED: now also IC8.P1, IC9.I2; no longer IC8.P3, IC9.I4
- net ENA_RADLED: now also IC8.P0, IC9.I1; no longer IC8.P1, IC9.I2
- net ENA_SCHRANKE: now also IC8.P7, IC9.I8; no longer IC8.P2, IC9.I3
- net ESP_GPIO0: now also ESP-01.GPIO0, ESP-12.GPIO0; no longer IC11.GPIO0
- net ESP_GPIO2: now also ESP-01.GPIO2, ESP-12.GPIO2; no longer IC11.GPIO2
- net GND: now also C32.2, ESP-01.GND, ESP-12.GND, J16.2, J18.1, J6.1, R26.1, R37.A, R9.1, T1.E; no longer IC11.GND, J16.1, J21.1, J23.1, R37.2, R38.2, R40.2, R42.2, R59.E, R60.1, R9.2, U2.C, U2.EMI
- net LINE_IN: now also R37.E; no longer R59.A
- net MOT_L_DIR: now also IC6.40; no longer IC6.29/PWM/T/ALT-CAN0TX
- net MOT_R_DIR: now also IC6.41; no longer IC6.30/PWM/T/ALT-CAN0RX
- net N$1: now also R36.2; no longer R36.1
- net N$13: now also IC7.P2, LED6.C; no longer IC5A.-IN, R17.2
- net N$14: now also R23.1; no longer R23.2
- net N$16: now also LED8.C; no longer R49.1
- net N$163: now also R37.S; no longer R59.S
- net N$17: now also IC7.P5, LED9.C; no longer IC7.P3, R48.1
- net N$18: now also IC7.P6, LED10.C; no longer IC7.P2, R47.1
- net N$19: now also IC7.P7, LED11.C; no longer IC7.P1, R46.1
- net N$2: now also R6.1; no longer R6.2
- net N$20: now also LED11.A, R52.2; no longer IC7.P0, R45.1
- net N$21: now also LED10.A, R51.2; no longer IC7.P5, R50.1
- net N$22: now also LED9.A, R50.2; no longer IC7.P6, R51.1
- net N$23: now also LED8.A, R49.2; no longer IC7.P7, R52.1
- net N$25: now also LED6.A, R47.2; no longer LED11.C, R52.2
- net N$26: now also LED5.A, R46.2; no longer LED4.C, R45.2
- net N$27: now also LED4.A, R45.2; no longer LED5.C, R46.2
- net N$28: now also LED12.A, R10.1; no longer LED6.C, R47.2
- net N$29: now also R11.2, T1.B; no longer LED7.C, R48.2
- net N$30: now also LED12.C, T1.C; no longer LED8.C, R49.2
- net N$38: now also R1.1; no longer R1.2
- net N$4: now also R8.1, R9.2; no longer R8.2, R9.1
- net N$6: now also IC7.P0, LED4.C; no longer LED2.A, R5.2
- net PWR_SERVO: no longer J3.2, R26.2
- net ROSC: now also R26.2; no longer R60.2
- net RX5: now also ESP-01.UTXD, ESP-12.TXD; no longer IC11.TXD
- net SCHRANKE: now also R43.1; no longer R43.2
- net SCHRANKE_3V3: now also IC6.46/SCK2, J20.2, R43.2; no longer IC6.54/CS2-1, R43.1
- net SERVO2_FB: now also IC6.23/A9/PWM/T; no longer IC6.49/A23/PWM
- net TX5: now also ESP-01.URXD, ESP-12.RXD; no longer IC11.RXD
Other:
- note added: "(Option A)"
- note added: "(Option B)"
- note added: "(o.ä. Reset-Controller)"
- note added: "Hinweis: Polung an Schraubklemme AK500-2-H vertauscht: jetzt identisch mit J25 Part in EAGLE Library con-ptr500 überführt"
- note added: "RPI_SPI0_CE1 RPI_GPIO26 SERVO3_PWM RPI_3V3"
- note added: "Rev. 0.6"
- note added: "WIFI-Modul (optional)"
- note removed: "(oder ähnlicher Reset-Controller)"
- note removed: "MAUS_SDIO als VCC fuer neuen Sensor MAUS_CLK als CS fuer neuen Sensor"
- note removed: "Rev. 0.5"
- note removed: "WIFI"
- note removed: "Wi-Fi Modul?"
- note removed: "Widerstandswerte an LEDs anpassen!"
- note removed: "max. 18V Eingangsspannung!"
- moved on the sheet: BT1, C1, C10, C11, C12, C13, C14, C15, C16, C17, C18, C19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
